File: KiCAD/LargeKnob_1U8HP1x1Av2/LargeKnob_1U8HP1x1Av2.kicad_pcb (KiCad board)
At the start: 2 copper layers, 40.3 x 39.7 mm, 5 parts

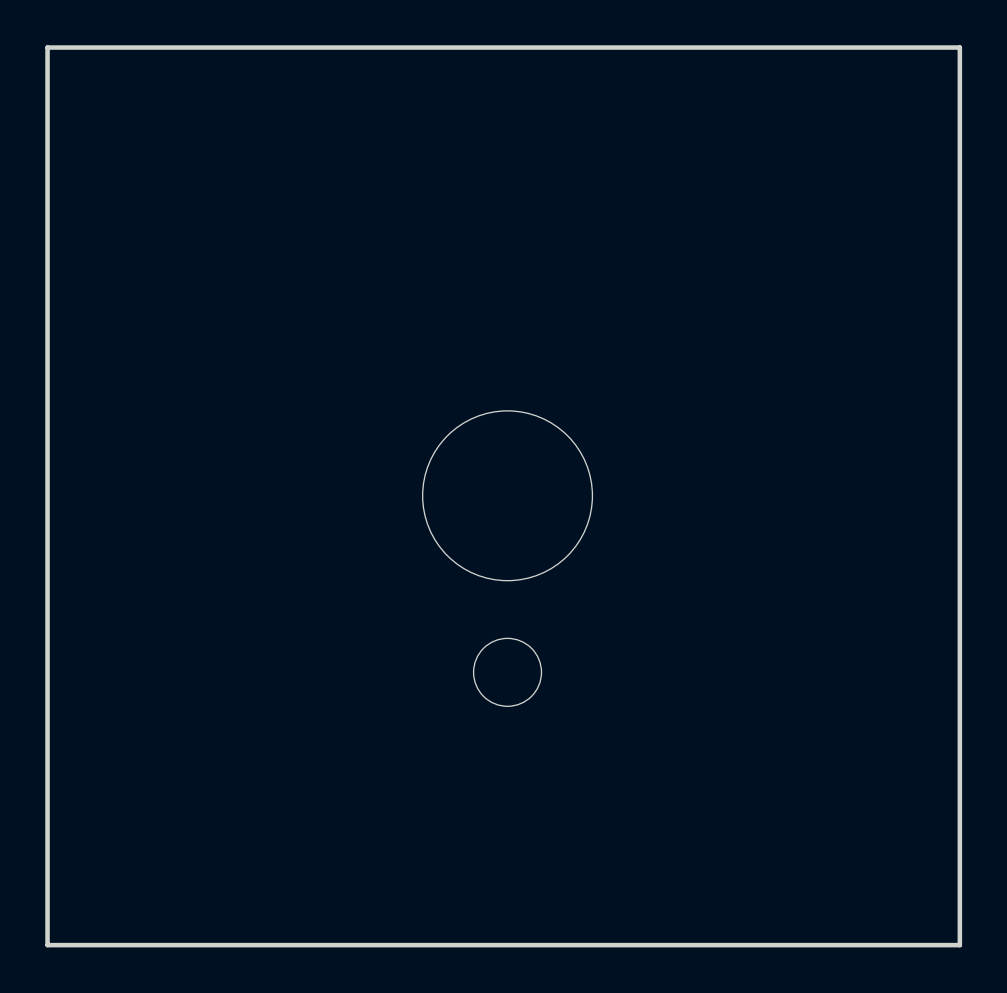
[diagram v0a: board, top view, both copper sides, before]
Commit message: updated all modules to use plated through-holes wherever possible
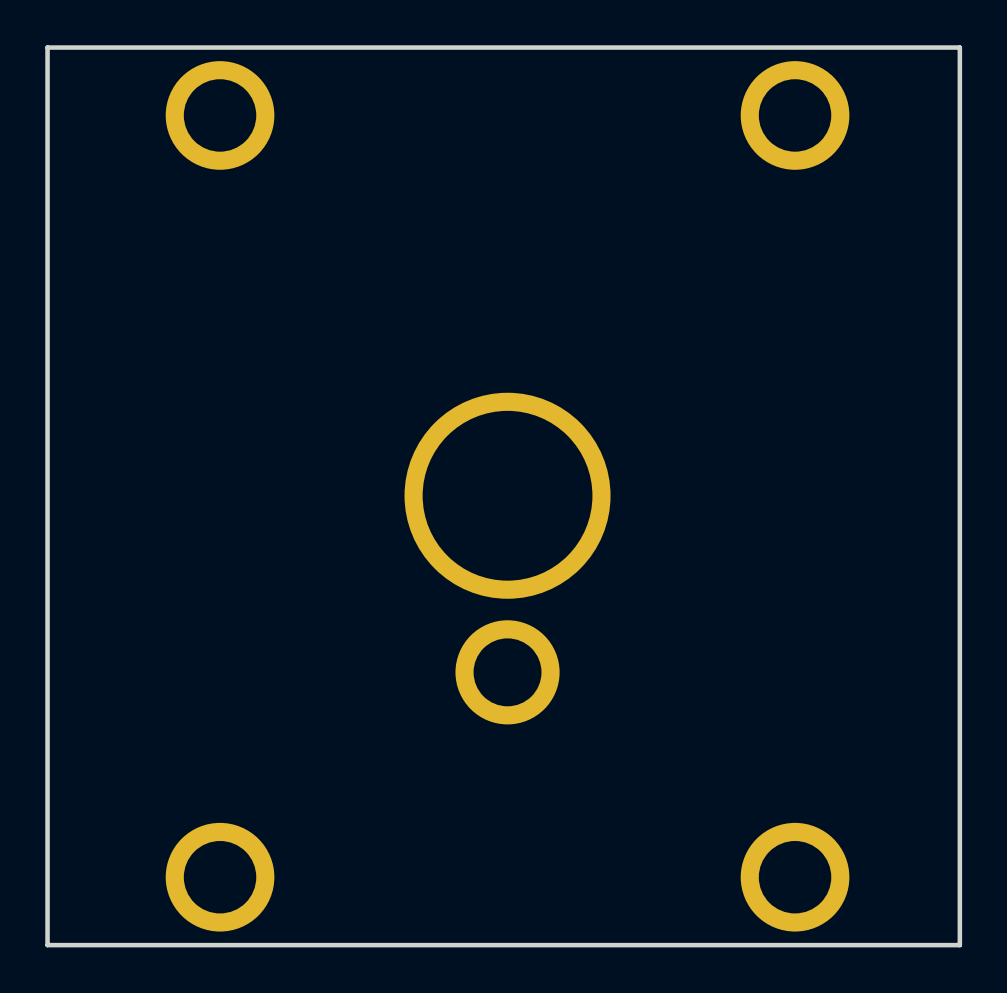
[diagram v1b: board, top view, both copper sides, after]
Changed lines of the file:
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@@
 			)
 		)
-		(pad "" np_thru_hole oval
+		(pad "" thru_hole circle
 			(at 0 0)
-			(size 4.34 3.2)
-			(drill oval 4.34 3.2)
-			(layers "*.Cu" "*.Mask")
+			(size 4.8 4.8)
+			(drill 3.2)
+			(layers "*.Cu" "*.Mask")
+			(remove_unused_layers no)
 		)
 		(embedded_fonts no)
@@
 			)
 		)
-		(pad "" np_thru_hole oval
+		(pad "" thru_hole circle
 			(at 0 0)
-			(size 4.34 3.2)
-			(drill oval 4.34 3.2)
-			(layers "*.Cu" "*.Mask")
+			(size 4.8 4.8)
+			(drill 3.2)
+			(layers "*.Cu" "*.Mask")
+			(remove_unused_layers no)
 		)
 		(embedded_fonts no)
@@
 		(at 20.32 22.225)
 		(property "Reference" "RP1"
-			(at 0 -4.975 0)
+			(at -0.07 -5.725 0)
 			(unlocked yes)
 			(layer "B.SilkS")
@@
 		)
 		(property "Value" "M7_Panel_Mount_Rotary_Potentiometer"
-			(at 0 10 0)
+			(at 0 11.025 0)
 			(unlocked yes)
 			(layer "F.Fab")
@@
 		)
 		(fp_text user "${REFERENCE}"
-			(at 0 -4.975 0)
-			(unlocked yes)
-			(layer "F.Fab")
-			(effects
-				(font
-					(size 1 1)
-					(thickness 0.15)
-				)
-			)
-		)
-		(pad "" np_thru_hole circle
+			(at 0 -5.725 0)
+			(unlocked yes)
+			(layer "F.Fab")
+			(effects
+				(font
+					(size 1 1)
+					(thickness 0.15)
+				)
+			)
+		)
+		(pad "" thru_hole circle
 			(at 0 0)
-			(size 7.5 7.5)
+			(size 9.1 9.1)
 			(drill 7.5)
 			(layers "*.Cu" "*.Mask")
-		)
-		(pad "" np_thru_hole circle
+			(remove_unused_layers no)
+		)
+		(pad "" thru_hole circle
 			(at 0 7.8)
-			(size 3 3)
+			(size 4.6 4.6)
 			(drill 3)
 			(layers "*.Cu" "*.Mask")
+			(remove_unused_layers no)
 		)
 		(embedded_fonts no)
@@
 			)
 		)
-		(pad "" np_thru_hole oval
+		(pad "" thru_hole circle
 			(at 0 0)
-			(size 4.34 3.2)
-			(drill oval 4.34 3.2)
-			(layers "*.Cu" "*.Mask")
+			(size 4.8 4.8)
+			(drill 3.2)
+			(layers "*.Cu" "*.Mask")
+			(remove_unused_layers no)
 		)
 		(embedded_fonts no)
@@
 			)
 		)
-		(pad "" np_thru_hole oval
+		(pad "" thru_hole circle
 			(at 0 0)
-			(size 4.34 3.2)
-			(drill oval 4.34 3.2)
-			(layers "*.Cu" "*.Mask")
+			(size 4.8 4.8)
+			(drill 3.2)
+			(layers "*.Cu" "*.Mask")
+			(remove_unused_layers no)
 		)
 		(embedded_fonts no)
